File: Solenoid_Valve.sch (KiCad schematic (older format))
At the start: 59 parts, among them IC1 Si8621AB-B-ISR, J1 Bus_mechaken_PCIexpress_x16_1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, J10 Conn_01x02, J11 Conn_01x02, J12 Conn_01x02, J13 Conn_01x02, J14 Conn_01x02, J15 Conn_01x02, J16 Conn_01x02, J17 Conn_01x02, J18 Conn_01x02, J19 Conn_01x02, J2 Conn_01x05, J20 Conn_01x02, J3 Conn_01x02, J4 Conn_01x02, J5 Conn_01x02, J6 Conn_01x02, J7 Conn_01x03, J8 Conn_01x02, J9 Conn_01x02, Q1 ULN2004D1013TR, Q2 ULN2004D1013TR, Q3 ULN2004D1013TR, U1 LDL1117S33R, U2 STM32F042K6Tx, U3 MCP2562-E-SN, U4 L7812, U5 LDL1117S33R

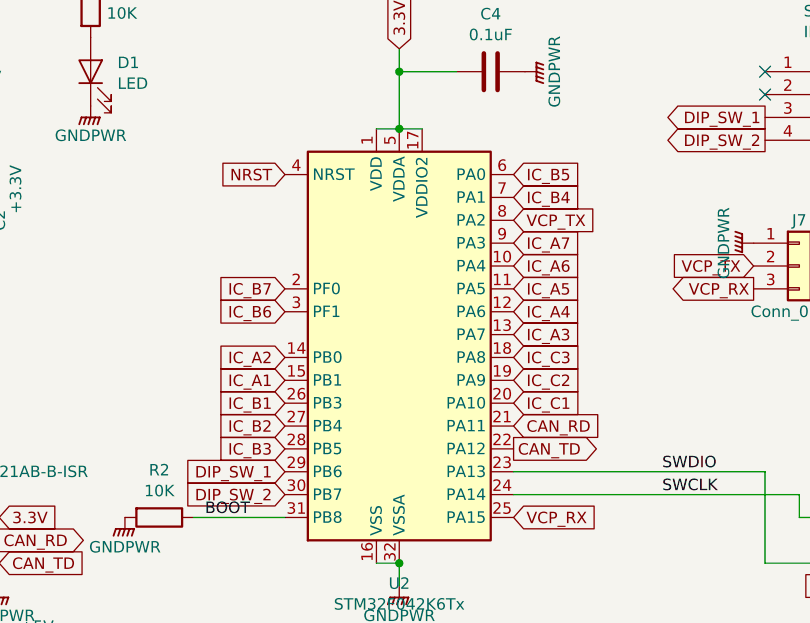
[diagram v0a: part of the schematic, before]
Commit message: fix
BOOT0の配線を修正
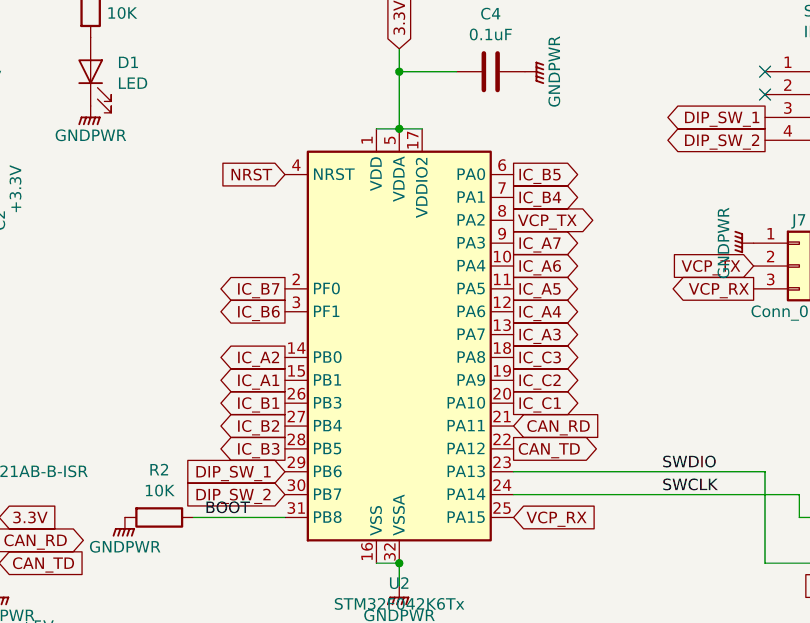
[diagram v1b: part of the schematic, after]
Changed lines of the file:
@@
 Text GLabel 5250 2100 0    50   Output ~ 0
 VCP_RX
-Text GLabel 4200 1800 2    50   Input ~ 0
-VCP_TX
 $Comp
 L Device:C C1
@@
 	1    0    0    -1
 $EndComp
-Text GLabel 3200 2500 0    50   Input ~ 0
+Text GLabel 3200 2500 0    50   Output ~ 0
 IC_A1
-Text GLabel 3200 2400 0    50   Input ~ 0
+Text GLabel 3200 2400 0    50   Output ~ 0
 IC_A2
-Text GLabel 4200 2300 2    50   Input ~ 0
-IC_A3
-Text GLabel 4200 2200 2    50   Input ~ 0
-IC_A4
-Text GLabel 4200 2100 2    50   Input ~ 0
-IC_A5
-Text GLabel 4200 2000 2    50   Input ~ 0
-IC_A6
-Text GLabel 4200 1900 2    50   Input ~ 0
-IC_A7
-Text GLabel 3200 2600 0    50   Input ~ 0
+Text GLabel 3200 2600 0    50   Output ~ 0
 IC_B1
-Text GLabel 3200 2700 0    50   Input ~ 0
+Text GLabel 3200 2700 0    50   Output ~ 0
 IC_B2
-Text GLabel 3200 2800 0    50   Input ~ 0
+Text GLabel 3200 2800 0    50   Output ~ 0
 IC_B3
-Text GLabel 4200 1700 2    50   Input ~ 0
-IC_B4
-Text GLabel 4200 1600 2    50   Input ~ 0
-IC_B5
-Text GLabel 3200 2200 0    50   Input ~ 0
+Text GLabel 3200 2200 0    50   Output ~ 0
 IC_B6
-Text GLabel 3200 2100 0    50   Input ~ 0
+Text GLabel 3200 2100 0    50   Output ~ 0
 IC_B7
-Text GLabel 4200 2600 2    50   Input ~ 0
-IC_C1
-Text GLabel 4200 2500 2    50   Input ~ 0
-IC_C2
-Text GLabel 4200 2400 2    50   Input ~ 0
-IC_C3
 $Comp
 L power:GNDPWR #PWR0120
@@
 NoConn ~ 5300 1250
 $Comp
-L power:GNDPWR #PWR?
+L power:GNDPWR #PWR0116
 U 1 1 5E334F41
 P 2500 3100
-F 0 "#PWR?" H 2500 2900 50  0001 C CNN
+F 0 "#PWR0116" H 2500 2900 50  0001 C CNN
 F 1 "GNDPWR" H 2500 2970 50  0000 C CNN
 F 2 "" H 2500 3050 50  0001 C CNN
@@
 	1    0    0    -1
 $EndComp
+Text GLabel 4200 2400 2    50   Output ~ 0
+IC_C3
+Text GLabel 4200 2500 2    50   Output ~ 0
+IC_C2
+Text GLabel 4200 2600 2    50   Output ~ 0
+IC_C1
+Text GLabel 4200 1600 2    50   Output ~ 0
+IC_B5
+Text GLabel 4200 1700 2    50   Output ~ 0
+IC_B4
+Text GLabel 4200 1900 2    50   Output ~ 0
+IC_A7
+Text GLabel 4200 2000 2    50   Output ~ 0
+IC_A6
+Text GLabel 4200 2100 2    50   Output ~ 0
+IC_A5
+Text GLabel 4200 2200 2    50   Output ~ 0
+IC_A4
+Text GLabel 4200 2300 2    50   Output ~ 0
+IC_A3
+Text GLabel 4200 1800 2    50   Output ~ 0
+VCP_TX
 $EndSCHEMATC

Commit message: change
フットプリントを手はんだ用に変更
レギュレーター保護用のダイオードを追加
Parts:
- removed D1: LED, Diode_SMD:D_0603_1608Metric, symbol Device:LED
- removed R1: 10K, Resistor_SMD:R_0603_1608Metric, symbol Device:R
- added D18: D_Schottky, Diode_SMD:D_0603_1608Metric_Pad1.05x0.95mm_HandSolder, symbol Device:D_Schottky
- C1: renamed from C5; footprint Capacitor_SMD:C_0805_2012Metric -> Capacitor_SMD:C_0805_2012Metric_Pad1.15x1.40mm_HandSolder
- C2: renamed from C1; footprint Capacitor_SMD:C_0805_2012Metric -> Capacitor_SMD:C_0805_2012Metric_Pad1.15x1.40mm_HandSolder
- C3: renamed from C2; footprint Capacitor_SMD:C_0805_2012Metric -> Capacitor_SMD:C_0805_2012Metric_Pad1.15x1.40mm_HandSolder
- C4: renamed from C6; footprint Capacitor_SMD:C_0805_2012Metric -> Capacitor_SMD:C_0805_2012Metric_Pad1.15x1.40mm_HandSolder
- C5: renamed from C9; footprint Capacitor_SMD:C_0805_2012Metric -> Capacitor_SMD:C_0805_2012Metric_Pad1.15x1.40mm_HandSolder
- C6: renamed from C4; footprint Capacitor_SMD:C_0805_2012Metric -> Capacitor_SMD:C_0805_2012Metric_Pad1.15x1.40mm_HandSolder
- C7: renamed from C10; footprint Capacitor_SMD:C_0805_2012Metric -> Capacitor_SMD:C_0805_2012Metric_Pad1.15x1.40mm_HandSolder
- C9: renamed from C8; footprint Capacitor_SMD:C_0805_2012Metric -> Capacitor_SMD:C_0805_2012Metric_Pad1.15x1.40mm_HandSolder
- D1: renamed from D2; footprint Diode_SMD:D_2010_5025Metric -> Diode_SMD:D_2010_5025Metric_Pad1.52x2.65mm_HandSolder
- D10: renamed from D12; footprint Diode_SMD:D_2010_5025Metric -> Diode_SMD:D_2010_5025Metric_Pad1.52x2.65mm_HandSolder
- D11: renamed from D13; footprint Diode_SMD:D_2010_5025Metric -> Diode_SMD:D_2010_5025Metric_Pad1.52x2.65mm_HandSolder
- D12: renamed from D14; footprint Diode_SMD:D_2010_5025Metric -> Diode_SMD:D_2010_5025Metric_Pad1.52x2.65mm_HandSolder
- D13: renamed from D15; footprint Diode_SMD:D_2010_5025Metric -> Diode_SMD:D_2010_5025Metric_Pad1.52x2.65mm_HandSolder
- D14: renamed from D16; footprint Diode_SMD:D_2010_5025Metric -> Diode_SMD:D_2010_5025Metric_Pad1.52x2.65mm_HandSolder
- D15: renamed from D17; footprint Diode_SMD:D_2010_5025Metric -> Diode_SMD:D_2010_5025Metric_Pad1.52x2.65mm_HandSolder
- D16: renamed from D18; footprint Diode_SMD:D_2010_5025Metric -> Diode_SMD:D_2010_5025Metric_Pad1.52x2.65mm_HandSolder
- D17: renamed from D19; footprint Diode_SMD:D_2010_5025Metric -> Diode_SMD:D_2010_5025Metric_Pad1.52x2.65mm_HandSolder
- D2: renamed from D3; footprint Diode_SMD:D_2010_5025Metric -> Diode_SMD:D_2010_5025Metric_Pad1.52x2.65mm_HandSolder
- D3: renamed from D4; footprint Diode_SMD:D_2010_5025Metric -> Diode_SMD:D_2010_5025Metric_Pad1.52x2.65mm_HandSolder
- D4: renamed from D6; footprint Diode_SMD:D_2010_5025Metric -> Diode_SMD:D_2010_5025Metric_Pad1.52x2.65mm_HandSolder
- D5: renamed from D7; footprint Diode_SMD:D_2010_5025Metric -> Diode_SMD:D_2010_5025Metric_Pad1.52x2.65mm_HandSolder
- D6: renamed from D8; footprint Diode_SMD:D_2010_5025Metric -> Diode_SMD:D_2010_5025Metric_Pad1.52x2.65mm_HandSolder
- D7: renamed from D9; footprint Diode_SMD:D_2010_5025Metric -> Diode_SMD:D_2010_5025Metric_Pad1.52x2.65mm_HandSolder
- D8: renamed from D10; footprint Diode_SMD:D_2010_5025Metric -> Diode_SMD:D_2010_5025Metric_Pad1.52x2.65mm_HandSolder
- D9: renamed from D11; footprint Diode_SMD:D_2010_5025Metric -> Diode_SMD:D_2010_5025Metric_Pad1.52x2.65mm_HandSolder
- R1: renamed from R2; footprint Resistor_SMD:R_0603_1608Metric -> Resistor_SMD:R_0603_1608Metric_Pad1.05x0.95mm_HandSolder
- U5: renamed from U4; value L7812 -> NJM7812
- renumbered C7 to C8, J4 to J2, J5 to J3, J7 to J4, J2 to J5, J8 to J7, J3 to J8, U3 to U2, U2 to U3, U5 to U4
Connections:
- net 3.3V: now also D18.2 (A)
- net VCC: now also D18.1 (K)
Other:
- moved on the sheet: C5, C7, U4
